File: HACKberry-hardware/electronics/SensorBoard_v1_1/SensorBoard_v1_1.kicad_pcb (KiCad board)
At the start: 2 copper layers, 20 x 20 mm, 4 parts, among them J1 ST-PJ-312, U1 QRE1113GR

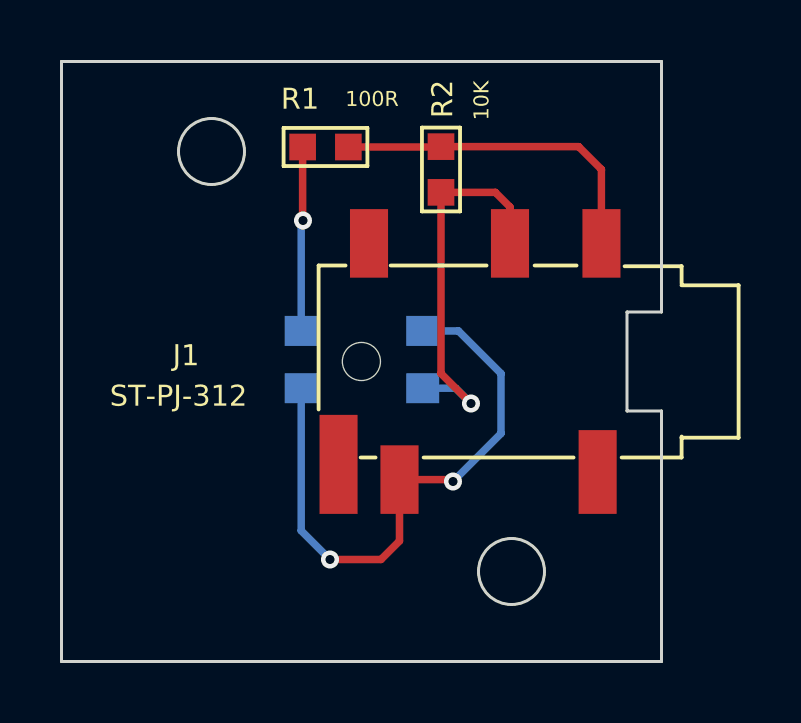
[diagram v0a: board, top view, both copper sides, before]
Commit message: Updated the PCB files for PCB manufacturing service.
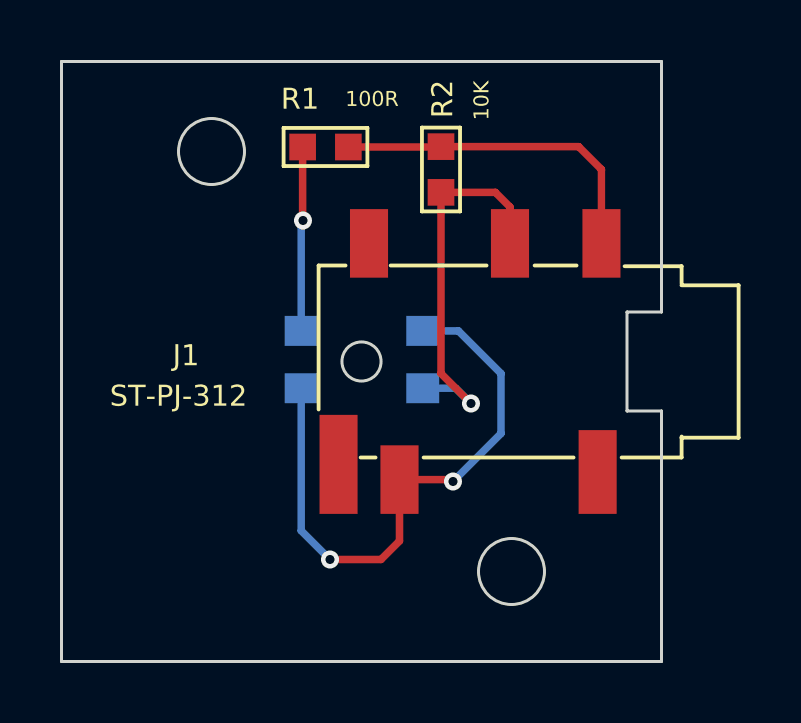
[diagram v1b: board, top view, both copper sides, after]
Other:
- outline, holes or cut-outs redrawn
- rule pad_to_mask_clearance: 0 -> 0.1
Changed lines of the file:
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@@
-(kicad_pcb (version 4) (host pcbnew "(after 2015-may-01 BZR unknown)-product")
+(kicad_pcb (version 4) (host pcbnew 4.0.1-stable)
   (general
     (links 7)
@@
     (area 110.199999 79.499999 133.083501 99.650001)
     (thickness 1.6)
-    (drawings 16)
+    (drawings 17)
     (tracks 31)
     (zones 0)
@@
     (pad_size 1.5 1.5)
     (pad_drill 0.6)
-    (pad_to_mask_clearance 0)
+    (pad_to_mask_clearance 0.1)
+    (solder_mask_min_width 0.1)
     (aux_axis_origin 0 0)
     (visible_elements 7FFFFFFF)
     (pcbplotparams
-      (layerselection 0x01030_80000001)
-      (usegerberextensions false)
+      (layerselection 0x010f0_80000001)
+      (usegerberextensions true)
       (excludeedgelayer true)
       (linewidth 0.100000)
@@
       (psnegative false)
       (psa4output false)
-      (plotreference true)
-      (plotvalue true)
+      (plotreference false)
+      (plotvalue false)
       (plotinvisibletext false)
       (padsonsilk false)
       (subtractmaskfromsilk false)
-      (outputformat 3)
+      (outputformat 1)
       (mirror false)
       (drillshape 0)
       (scaleselection 1)
-      (outputdirectory ../../../../../../Desktop/))
+      (outputdirectory 160111SensorBoard_v1_1/))
   )
   (net 0 "")
@@
     (pad COM1 smd rect (at 3.048 -3.937 90) (size 2.286 1.27) (layers F.Cu F.Paste F.Mask)
       (net 6 VCC) (solder_mask_margin 0.2))
-    (pad Hole np_thru_hole circle (at -4.953 0) (size 1.27 1.27) (drill 1.27) (layers))
   )
   (module SMD-RES-100R-5_-1_10W_0603_:R0603 (layer F.Cu)
@@
       (net 2 GND) (solder_mask_margin 0.2))
   )
+  (gr_circle (center 120.25 89.55) (end 120.3 88.9) (layer Edge.Cuts) (width 0.1))
   (gr_circle (center 115.25 82.55) (end 116.35 82.55) (layer Edge.Cuts) (width 0.1))
   (gr_circle (center 115.25 82.55) (end 117.25 82.55) (layer Eco1.User) (width 0.2))
